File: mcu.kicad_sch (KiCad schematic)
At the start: 40 parts, among them U1 STM32U5G9ZJTxQ, Y1 NX2016SA-16MHZ-EXS00A-CS07826, Y2 NX2012SA-32.768K-STD-MUB-1

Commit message: Place all components on the PCB correctly
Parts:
- added C28: 100n, Capacitor_SMD:C_0603_1608Metric_Pad1.08x0.95mm_HandSolder, symbol Device:C
- renumbered C28 to C29, C29 to C30, C30 to C31, C31 to C32, C32 to C33, C33 to C34, C34 to C35, C35 to C36
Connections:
- net 3V3_MCU: now also C28.1
- net GND: now also C28.2
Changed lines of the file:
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@@
 	)
 	(junction
+		(at 179.07 175.26)
+		(diameter 0)
+		(color 0 0 0 0)
+	)
+	(junction
 		(at 109.22 199.39)
 		(diameter 0)
@@
 	(wire
 		(pts
+			(xy 179.07 175.26) (xy 184.15 175.26)
+		)
+		(stroke
+			(width 0)
+			(type default)
+		)
+	)
+	(wire
+		(pts
 			(xy 238.76 59.69) (xy 238.76 62.23)
 		)
@@
 	(wire
 		(pts
-			(xy 170.18 175.26) (xy 177.8 175.26)
+			(xy 170.18 175.26) (xy 179.07 175.26)
 		)
 		(stroke
@@
 	)
 	(label "VDD"
-		(at 177.8 175.26 0)
+		(at 184.15 175.26 0)
 		(effects
 			(font
@@
 		(dnp no)
 		(fields_autoplaced yes)
-		(property "Reference" "#PWR048"
+		(property "Reference" "#PWR049"
 			(at 87.63 213.36 0)
 			(effects
@@
 			(project "weather-station-poc"
 				(path "/38eb53bb-294e-46e4-ad59-fd355ca373b9/5f00b1ab-9f48-4782-8810-a8d68b4e6a2f"
-					(reference "#PWR048")
+					(reference "#PWR049")
 					(unit 1)
 				)
@@
 		(dnp no)
 		(fields_autoplaced yes)
-		(property "Reference" "C35"
+		(property "Reference" "C36"
 			(at 97.79 252.7299 0)
 			(effects
@@
 			(project "weather-station-poc"
 				(path "/38eb53bb-294e-46e4-ad59-fd355ca373b9/5f00b1ab-9f48-4782-8810-a8d68b4e6a2f"
-					(reference "C35")
+					(reference "C36")
 					(unit 1)
 				)
@@
 		(dnp no)
 		(fields_autoplaced yes)
-		(property "Reference" "#PWR056"
+		(property "Reference" "#PWR057"
 			(at 76.2 264.16 0)
 			(effects
@@
 			(project "weather-station-poc"
 				(path "/38eb53bb-294e-46e4-ad59-fd355ca373b9/5f00b1ab-9f48-4782-8810-a8d68b4e6a2f"
-					(reference "#PWR056")
+					(reference "#PWR057")
 					(unit 1)
 				)
@@
 		(dnp no)
 		(fields_autoplaced yes)
-		(property "Reference" "#PWR053"
+		(property "Reference" "#PWR054"
 			(at 85.09 241.3 0)
 			(effects
@@
 			(project "weather-station-poc"
 				(path "/38eb53bb-294e-46e4-ad59-fd355ca373b9/5f00b1ab-9f48-4782-8810-a8d68b4e6a2f"
-					(reference "#PWR053")
+					(reference "#PWR054")
 					(unit 1)
 				)
@@
 		(dnp no)
 		(fields_autoplaced yes)
-		(property "Reference" "#PWR047"
+		(property "Reference" "#PWR048"
 			(at 76.2 213.36 0)
 			(effects
@@
 			(project "weather-station-poc"
 				(path "/38eb53bb-294e-46e4-ad59-fd355ca373b9/5f00b1ab-9f48-4782-8810-a8d68b4e6a2f"
-					(reference "#PWR047")
+					(reference "#PWR048")
 					(unit 1)
 				)
@@
 	)
 	(symbol
+		(lib_id "Device:C")
+		(at 179.07 179.07 0)
+		(unit 1)
+		(exclude_from_sim no)
+		(in_bom yes)
+		(on_board yes)
+		(dnp no)
+		(fields_autoplaced yes)
+		(property "Reference" "C28"
+			(at 182.88 177.7999 0)
+			(effects
+				(font
+					(size 1.27 1.27)
+				)
+				(justify left)
+			)
+		)
+		(property "Value" "100n"
+			(at 182.88 180.3399 0)
+			(effects
+				(font
+					(size 1.27 1.27)
+				)
+				(justify left)
+			)
+		)
+		(property "Footprint" "Capacitor_SMD:C_0603_1608Metric_Pad1.08x0.95mm_HandSolder"
+			(at 180.0352 182.88 0)
+			(effects
+				(font
+					(size 1.27 1.27)
+				)
+				(hide yes)
+			)
+		)
+		(property "Datasheet" "~"
+			(at 179.07 179.07 0)
+			(effects
+				(font
+					(size 1.27 1.27)
+				)
+				(hide yes)
+			)
+		)
+		(property "Description" "Unpolarized capacitor"
+			(at 179.07 179.07 0)
+			(effects
+				(font
+					(size 1.27 1.27)
+				)
+				(hide yes)
+			)
+		)
+		(pin "2"
+		)
+		(pin "1"
+		)
+		(instances
+			(project "weather-station-poc"
+				(path "/38eb53bb-294e-46e4-ad59-fd355ca373b9/5f00b1ab-9f48-4782-8810-a8d68b4e6a2f"
+					(reference "C28")
+					(unit 1)
+				)
+			)
+		)
+	)
+	(symbol
+		(lib_id "power:GND")
+		(at 179.07 182.88 0)
+		(unit 1)
+		(exclude_from_sim no)
+		(in_bom yes)
+		(on_board yes)
+		(dnp no)
+		(fields_autoplaced yes)
+		(property "Reference" "#PWR047"
+			(at 179.07 189.23 0)
+			(effects
+				(font
+					(size 1.27 1.27)
+				)
+				(hide yes)
+			)
+		)
+		(property "Value" "GND"
+			(at 179.07 187.96 0)
+			(effects
+				(font
+					(size 1.27 1.27)
+				)
+			)
+		)
+		(property "Footprint" ""
+			(at 179.07 182.88 0)
+			(effects
+				(font
+					(size 1.27 1.27)
+				)
+				(hide yes)
+			)
+		)
+		(property "Datasheet" ""
+			(at 179.07 182.88 0)
+			(effects
+				(font
+					(size 1.27 1.27)
+				)
+				(hide yes)
+			)
+		)
+		(property "Description" "Power symbol creates a global label with name \"GND\" , ground"
+			(at 179.07 182.88 0)
+			(effects
+				(font
+					(size 1.27 1.27)
+				)
+				(hide yes)
+			)
+		)
+		(pin "1"
+		)
+		(instances
+			(project "weather-station-poc"
+				(path "/38eb53bb-294e-46e4-ad59-fd355ca373b9/5f00b1ab-9f48-4782-8810-a8d68b4e6a2f"
+					(reference "#PWR047")
+					(unit 1)
+				)
+			)
+		)
+	)
+	(symbol
 		(lib_id "power:GND")
 		(at 109.22 207.01 0)
@@
 		(dnp no)
 		(fields_autoplaced yes)
-		(property "Reference" "#PWR050"
+		(property "Reference" "#PWR051"
 			(at 109.22 213.36 0)
 			(effects
@@
 			(project "weather-station-poc"
 				(path "/38eb53bb-294e-46e4-ad59-fd355ca373b9/5f00b1ab-9f48-4782-8810-a8d68b4e6a2f"
-					(reference "#PWR050")
+					(reference "#PWR051")
 					(unit 1)
 				)
@@
 		(dnp no)
 		(fields_autoplaced yes)
-		(property "Reference" "#PWR051"
+		(property "Reference" "#PWR052"
 			(at 85.09 218.44 0)
 			(effects
@@
 			(project "weather-station-poc"
 				(path "/38eb53bb-294e-46e4-ad59-fd355ca373b9/5f00b1ab-9f48-4782-8810-a8d68b4e6a2f"
-					(reference "#PWR051")
+					(reference "#PWR052")
 					(unit 1)
 				)
@@
 		(dnp no)
 		(fields_autoplaced yes)
-		(property "Reference" "C31"
+		(property "Reference" "C32"
 			(at 113.03 201.9299 0)
 			(effects
@@
 			(project "weather-station-poc"
 				(path "/38eb53bb-294e-46e4-ad59-fd355ca373b9/5f00b1ab-9f48-4782-8810-a8d68b4e6a2f"
-					(reference "C31")
+					(reference "C32")
 					(unit 1)
 				)
@@
 		(dnp no)
 		(fields_autoplaced yes)
-		(property "Reference" "C32"
+		(property "Reference" "C33"
 			(at 78.74 232.4099 0)
 			(effects
@@
 			(project ""
 				(path "/38eb53bb-294e-46e4-ad59-fd355ca373b9/5f00b1ab-9f48-4782-8810-a8d68b4e6a2f"
-					(reference "C32")
+					(reference "C33")
 					(unit 1)
 				)
@@
 		(dnp no)
 		(fields_autoplaced yes)
-		(property "Reference" "#PWR055"
+		(property "Reference" "#PWR056"
 			(at 93.98 243.84 0)
 			(effects
@@
 			(project "weather-station-poc"
 				(path "/38eb53bb-294e-46e4-ad59-fd355ca373b9/5f00b1ab-9f48-4782-8810-a8d68b4e6a2f"
-					(reference "#PWR055")
+					(reference "#PWR056")
 					(unit 1)
 				)
@@
 		(dnp no)
 		(fields_autoplaced yes)
-		(property "Reference" "#PWR052"
+		(property "Reference" "#PWR053"
 			(at 280.67 238.76 0)
 			(effects
@@
 			(project ""
 				(path "/38eb53bb-294e-46e4-ad59-fd355ca373b9/5f00b1ab-9f48-4782-8810-a8d68b4e6a2f"
-					(reference "#PWR052")
+					(reference "#PWR053")
 					(unit 1)
 				)
@@
 		(dnp no)
 		(fields_autoplaced yes)
-		(property "Reference" "#PWR049"
+		(property "Reference" "#PWR050"
 			(at 97.79 213.36 0)
 			(effects
@@
 			(project "weather-station-poc"
 				(path "/38eb53bb-294e-46e4-ad59-fd355ca373b9/5f00b1ab-9f48-4782-8810-a8d68b4e6a2f"
-					(reference "#PWR049")
+					(reference "#PWR050")
 					(unit 1)
 				)
@@
 		(dnp no)
 		(fields_autoplaced yes)
-		(property "Reference" "#PWR057"
+		(property "Reference" "#PWR058"
 			(at 93.98 264.16 0)
 			(effects
@@
 			(project "weather-station-poc"
 				(path "/38eb53bb-294e-46e4-ad59-fd355ca373b9/5f00b1ab-9f48-4782-8810-a8d68b4e6a2f"
-					(reference "#PWR057")
+					(reference "#PWR058")
 					(unit 1)
 				)
@@
 		(dnp no)
 		(fields_autoplaced yes)
-		(property "Reference" "C33"
+		(property "Reference" "C34"
 			(at 97.79 232.4099 0)
 			(effects
@@
 			(project "weather-station-poc"
 				(path "/38eb53bb-294e-46e4-ad59-fd355ca373b9/5f00b1ab-9f48-4782-8810-a8d68b4e6a2f"
-					(reference "C33")
+					(reference "C34")
 					(unit 1)
 				)
@@
 		(dnp no)
 		(fields_autoplaced yes)
-		(property "Reference" "#PWR054"
+		(property "Reference" "#PWR055"
 			(at 74.93 243.84 0)
 			(effects
@@
 			(project "weather-station-poc"
 				(path "/38eb53bb-294e-46e4-ad59-fd355ca373b9/5f00b1ab-9f48-4782-8810-a8d68b4e6a2f"
-					(reference "#PWR054")
+					(reference "#PWR055")
 					(unit 1)
 				)
@@
 		(dnp no)
 		(fields_autoplaced yes)
-		(property "Reference" "C29"
+		(property "Reference" "C30"
 			(at 91.44 201.9299 0)
 			(effects
@@
 			(project "weather-station-poc"
 				(path "/38eb53bb-294e-46e4-ad59-fd355ca373b9/5f00b1ab-9f48-4782-8810-a8d68b4e6a2f"
-					(reference "C29")
+					(reference "C30")
 					(unit 1)
 				)
@@
 		(dnp no)
 		(fields_autoplaced yes)
-		(property "Reference" "C28"
+		(property "Reference" "C29"
 			(at 80.01 201.9299 0)
 			(effects
@@
 			(project "weather-station-poc"
 				(path "/38eb53bb-294e-46e4-ad59-fd355ca373b9/5f00b1ab-9f48-4782-8810-a8d68b4e6a2f"
-					(reference "C28")
+					(reference "C29")
 					(unit 1)
 				)
@@
 		(dnp no)
 		(fields_autoplaced yes)
-		(property "Reference" "C30"
+		(property "Reference" "C31"
 			(at 101.6 201.9299 0)
 			(effects
@@
 			(project "weather-station-poc"
 				(path "/38eb53bb-294e-46e4-ad59-fd355ca373b9/5f00b1ab-9f48-4782-8810-a8d68b4e6a2f"
-					(reference "C30")
+					(reference "C31")
 					(unit 1)
 				)
@@
 		(dnp no)
 		(fields_autoplaced yes)
-		(property "Reference" "C34"
+		(property "Reference" "C35"
 			(at 80.01 252.7299 0)
 			(effects
@@
 			(project "weather-station-poc"
 				(path "/38eb53bb-294e-46e4-ad59-fd355ca373b9/5f00b1ab-9f48-4782-8810-a8d68b4e6a2f"
-					(reference "C34")
+					(reference "C35")
 					(unit 1)
 				)

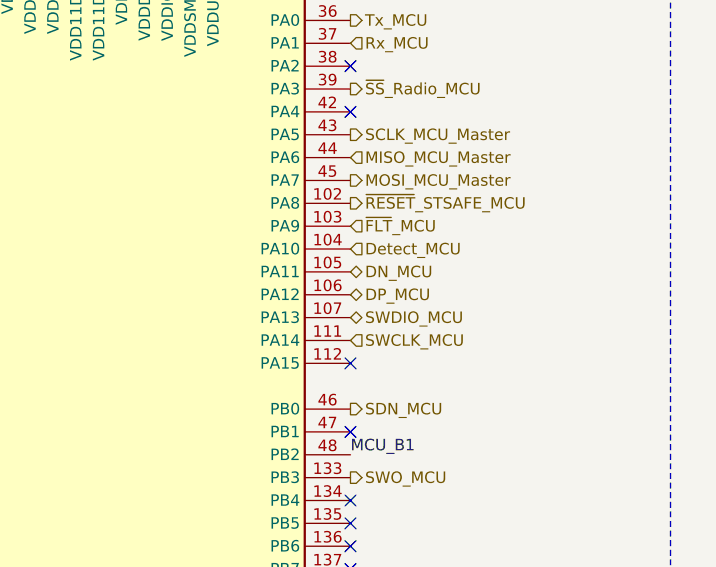
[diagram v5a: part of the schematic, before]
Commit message: Modify USB data signals name to trace diff pairs
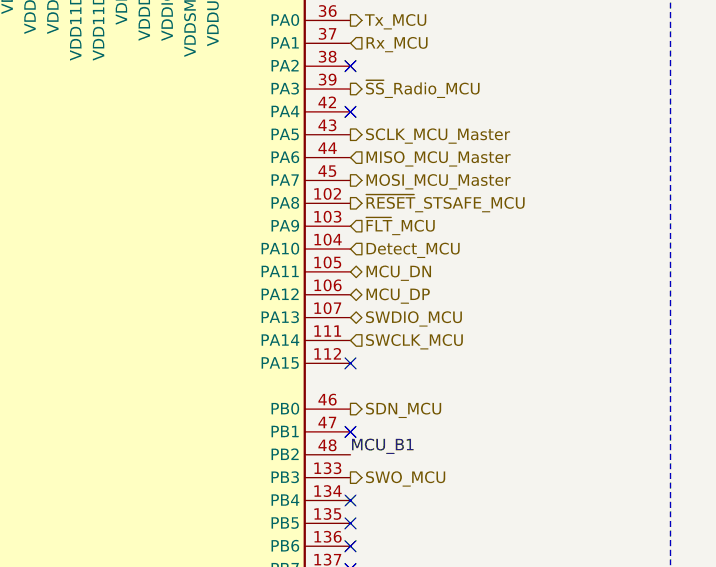
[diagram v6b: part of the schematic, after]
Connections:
- net DN_MCU renamed MCU_DN
- net DP_MCU renamed MCU_DP
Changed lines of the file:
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@@
 		)
 	)
-	(hierarchical_label "DN_MCU"
+	(hierarchical_label "MCU_DN"
 		(shape bidirectional)
 		(at 320.04 90.17 0)
@@
 		)
 	)
-	(hierarchical_label "DP_MCU"
+	(hierarchical_label "MCU_DP"
 		(shape bidirectional)
 		(at 320.04 92.71 0)

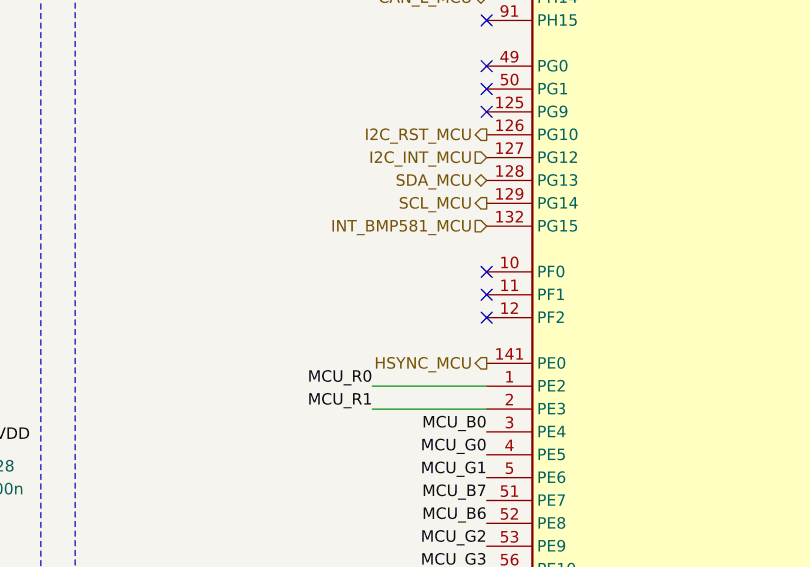
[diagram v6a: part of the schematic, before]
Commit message: Use I2C for slave MCU for bootloader
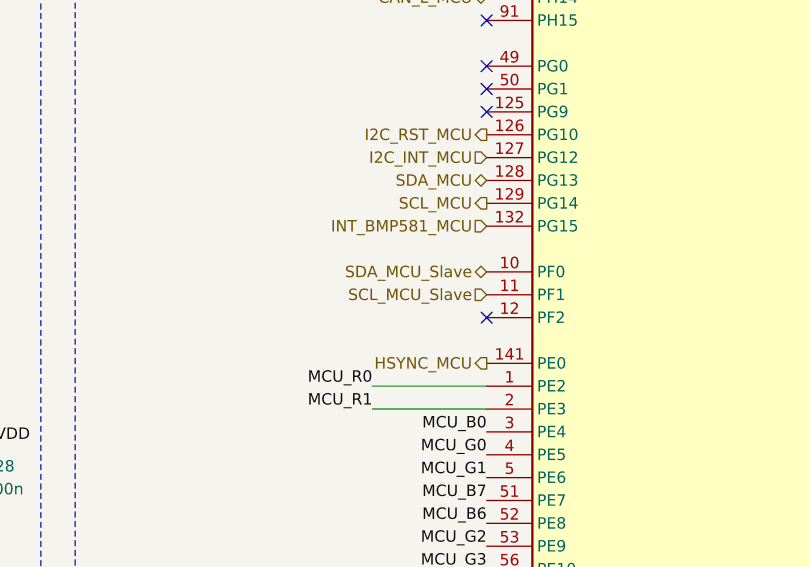
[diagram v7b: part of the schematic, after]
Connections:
- net SDA_MCU_Slave: now reaches U1.10 (PF0)
- net SCL_MCU_Slave: now reaches U1.11 (PF1)
- no-connect marks 45 -> 43
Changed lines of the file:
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@@
-	)
-	(no_connect
-		(at 238.76 156.21)
 	)
 	(no_connect
@@
 	(no_connect
 		(at 238.76 74.93)
-	)
-	(no_connect
-		(at 238.76 158.75)
 	)
 	(no_connect
@@
 		)
 	)
+	(hierarchical_label "SDA_MCU_Slave"
+		(shape bidirectional)
+		(at 238.76 156.21 180)
+		(effects
+			(font
+				(size 1.27 1.27)
+			)
+			(justify right)
+		)
+	)
 	(hierarchical_label "3V3_MCU"
 		(shape input)
@@
 		(effects
 			(font
+				(size 1.27 1.27)
+			)
+			(justify right)
+		)
+	)
+	(hierarchical_label "SCL_MCU_Slave"
+		(shape input)
+		(at 238.76 158.75 180)
+		(effects
+			(font

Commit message: Prepare PCB for routing
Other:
- note removed: "TODO: add debounce for button"
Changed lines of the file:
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@@
 	(text "RGB parallel bus"
 		(exclude_from_sim no)
-		(at 125.73 219.71 0)
-		(effects
-			(font
-				(size 1.27 1.27)
-			)
-		)
-	)
-	(text "TODO: add debounce for button"
-		(exclude_from_sim no)
-		(at 209.55 50.8 0)
+		(at 125.476 219.71 0)
 		(effects
 			(font
@@
 	(text "Crystal oscillators (HSE and LSE)"
 		(exclude_from_sim no)
-		(at 73.914 219.456 0)
+		(at 73.66 219.71 0)
 		(effects
 			(font
@@
 	(text "TODO: verify there is no error in pinout"
 		(exclude_from_sim no)
-		(at 213.36 236.22 0)
+		(at 208.534 237.49 0)
 		(effects
 			(font
@@
 	(text "STM32U5G9ZJTxQ MCU"
 		(exclude_from_sim no)
-		(at 204.47 41.91 0)
+		(at 201.93 41.91 0)
 		(effects
 			(font
@@
 	(text "STM32U5G9ZJTxQ decoupling capacitors"
 		(exclude_from_sim no)
-		(at 77.47 41.91 0)
+		(at 76.962 41.91 0)
 		(effects
 			(font
